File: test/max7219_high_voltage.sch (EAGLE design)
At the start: 11 parts, among them IC4 MAX7219CNG

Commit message: tschüüüüüs
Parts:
- removed NPN: 2N3904, transistor-npn:2N3904
- added NPN2: 2N3904, transistor-npn:2N3904
- added PNP1: 2N3906, transistor-pnp:2N3906
- added R2: 10k, resistor:R-EU_0204/7
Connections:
- new net N$6: NPN2.B, PNP1.C, R2.1
- net 3.3V: now also NPN2.E, R2.2; no longer NPN.E
- net N$1: now also NPN2.C; no longer NPN.C
- net N$2: now also PNP1.B; no longer NPN.B
- net VCC: now also PNP1.E

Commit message: Test Schematic updated
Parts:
- added G1: AB9V, battery:AB9V
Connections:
- new net N$5: G1.+, PNP.E, R1.1
- net VCC: now also G1.-; no longer PNP.E, R1.1
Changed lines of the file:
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@@
 <?xml version="1.0" encoding="utf-8"?>
 <!DOCTYPE eagle SYSTEM "eagle.dtd">
-<eagle version="9.6.2">
+<eagle version="9.0.1">
 <drawing>
 <settings>
@@
 <part name="C3" library="resistor" library_urn="urn:adsk.eagle:library:348" deviceset="C-EU" device="025-025X050" package3d_urn="urn:adsk.eagle:package:26151/1" value="10nF"/>
 <part name="GND10" library="SparkFun-PowerSymbols" library_urn="urn:adsk.eagle:library:530" deviceset="GND2" device=""/>
-<part name="18V" library="supply2" library_urn="urn:adsk.eagle:library:372" deviceset="VCC" device="" value="18V"/>
 <part name="PNP" library="transistor-pnp" deviceset="2N3906" device=""/>
 <part name="R1" library="resistor" library_urn="urn:adsk.eagle:library:348" deviceset="R-EU_" device="0204/7" package3d_urn="urn:adsk.eagle:package:25945/1" value="10k"/>
-<part name="18V1" library="supply2" library_urn="urn:adsk.eagle:library:372" deviceset="VCC" device="" value="18V"/>
 <part name="NPN1" library="transistor-npn" deviceset="2N3904" device=""/>
 <part name="GND3" library="SparkFun-PowerSymbols" library_urn="urn:adsk.eagle:library:530" deviceset="GND2" device=""/>
@@
 <part name="GND4" library="SparkFun-PowerSymbols" library_urn="urn:adsk.eagle:library:530" deviceset="GND2" device=""/>
 <part name="18V2" library="supply2" library_urn="urn:adsk.eagle:library:372" deviceset="VCC" device="" value="5V"/>
+<part name="G1" library="battery" library_urn="urn:adsk.eagle:library:109" deviceset="AB9V" device="" package3d_urn="urn:adsk.eagle:package:4600/1"/>
 </parts>
 <sheets>
@@
 <attribute name="VALUE" x="-217.9574" y="52.197" size="1.778" layer="96" rot="R270"/>
 </instance>
-<instance part="5V" gate="VCC" x="-205.74" y="60.96" smashed="yes">
-<attribute name="VALUE" x="-208.28" y="58.42" size="1.778" layer="96" rot="R90"/>
+<instance part="5V" gate="VCC" x="-198.12" y="53.34" smashed="yes" rot="R270">
+<attribute name="VALUE" x="-200.66" y="55.88" size="1.778" layer="96"/>
 </instance>
 <instance part="GND2" gate="G$1" x="-198.12" y="-33.02" smashed="yes">
@@
 <attribute name="VALUE" x="-225.298" y="53.34" size="1.778" layer="96" rot="R270" align="top-center"/>
 </instance>
-<instance part="18V" gate="G$1" x="-83.82" y="43.18" smashed="yes">
-<attribute name="VALUE" x="-85.725" y="46.355" size="1.778" layer="96"/>
-</instance>
 <instance part="PNP" gate="G$1" x="-86.36" y="33.02" smashed="yes">
-<attribute name="NAME" x="-96.52" y="40.64" size="1.778" layer="95"/>
-<attribute name="VALUE" x="-96.52" y="38.1" size="1.778" layer="96"/>
+<attribute name="NAME" x="-88.9" y="27.94" size="1.778" layer="95"/>
+<attribute name="VALUE" x="-88.9" y="35.56" size="1.778" layer="96"/>
 </instance>
 <instance part="R1" gate="G$1" x="-91.44" y="25.4" smashed="yes" rot="R90">
@@
 <attribute name="VALUE" x="-88.138" y="21.59" size="1.778" layer="96" rot="R90"/>
 </instance>
-<instance part="18V1" gate="G$1" x="-91.44" y="15.24" smashed="yes" rot="R180">
-<attribute name="VALUE" x="-89.535" y="12.065" size="1.778" layer="96" rot="R180"/>
-</instance>
 <instance part="NPN1" gate="G1" x="-99.06" y="33.02" smashed="yes">
-<attribute name="NAME" x="-109.22" y="40.64" size="1.778" layer="95"/>
-<attribute name="VALUE" x="-109.22" y="38.1" size="1.778" layer="96"/>
+<attribute name="NAME" x="-104.14" y="27.94" size="1.778" layer="95"/>
+<attribute name="VALUE" x="-104.14" y="35.56" size="1.778" layer="96"/>
 </instance>
 <instance part="GND3" gate="G$1" x="-99.06" y="22.86" smashed="yes" rot="R270">
@@
 <attribute name="VALUE" x="-98.425" y="5.715" size="1.778" layer="96"/>
 </instance>
+<instance part="G1" gate="G$1" x="-180.34" y="66.04"/>
 </instances>
 <busses>
@@
 <pinref part="5V" gate="VCC" pin="VCC"/>
 <pinref part="MODUL1" gate="MODUL" pin="+5V"/>
-<wire x1="-205.74" y1="58.42" x2="-205.74" y2="53.34" width="0.1524" layer="91"/>
+<wire x1="-200.66" y1="53.34" x2="-205.74" y2="53.34" width="0.1524" layer="91"/>
 <pinref part="C2" gate="G$1" pin="+"/>
 <wire x1="-205.74" y1="53.34" x2="-205.74" y2="43.18" width="0.1524" layer="91"/>
 <wire x1="-210.82" y1="53.34" x2="-205.74" y2="53.34" width="0.1524" layer="91"/>
 <junction x="-205.74" y="53.34"/>
-</segment>
-<segment>
-<wire x1="-91.44" y1="20.32" x2="-91.44" y2="17.78" width="0.1524" layer="91"/>
-<pinref part="R1" gate="G$1" pin="1"/>
-<junction x="-91.44" y="20.32"/>
-<pinref part="18V1" gate="G$1" pin="VCC"/>
-<junction x="-91.44" y="17.78"/>
-</segment>
-<segment>
-<pinref part="18V" gate="G$1" pin="VCC"/>
-<pinref part="PNP" gate="G$1" pin="E"/>
-<wire x1="-83.82" y1="40.64" x2="-83.82" y2="38.1" width="0.1524" layer="91"/>
-<junction x="-83.82" y="38.1"/>
-<junction x="-83.82" y="40.64"/>
+<wire x1="-205.74" y1="53.34" x2="-205.74" y2="66.04" width="0.1524" layer="91"/>
+<pinref part="G1" gate="G$1" pin="-"/>
+<wire x1="-205.74" y1="66.04" x2="-193.04" y2="66.04" width="0.1524" layer="91"/>
 </segment>
 <segment>
@@
 </segment>
 </net>
+<net name="N$5" class="0">
+<segment>
+<pinref part="G1" gate="G$1" pin="+"/>
+<wire x1="-167.64" y1="66.04" x2="-76.2" y2="66.04" width="0.1524" layer="91"/>
+<wire x1="-76.2" y1="66.04" x2="-76.2" y2="38.1" width="0.1524" layer="91"/>
+<pinref part="PNP" gate="G$1" pin="E"/>
+<wire x1="-76.2" y1="38.1" x2="-83.82" y2="38.1" width="0.1524" layer="91"/>
+<wire x1="-76.2" y1="38.1" x2="-76.2" y2="17.78" width="0.1524" layer="91"/>
+<junction x="-76.2" y="38.1"/>
+<wire x1="-91.44" y1="20.32" x2="-91.44" y2="17.78" width="0.1524" layer="91"/>
+<pinref part="R1" gate="G$1" pin="1"/>
+<junction x="-91.44" y="20.32"/>
+<wire x1="-76.2" y1="17.78" x2="-91.44" y2="17.78" width="0.1524" layer="91"/>
+</segment>
+</net>

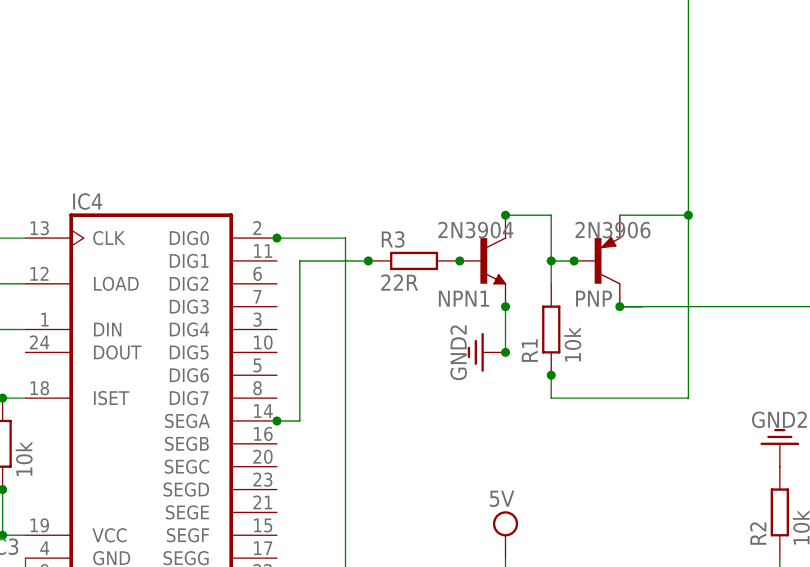
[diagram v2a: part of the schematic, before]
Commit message: test 2k2Ohm ansatt 220
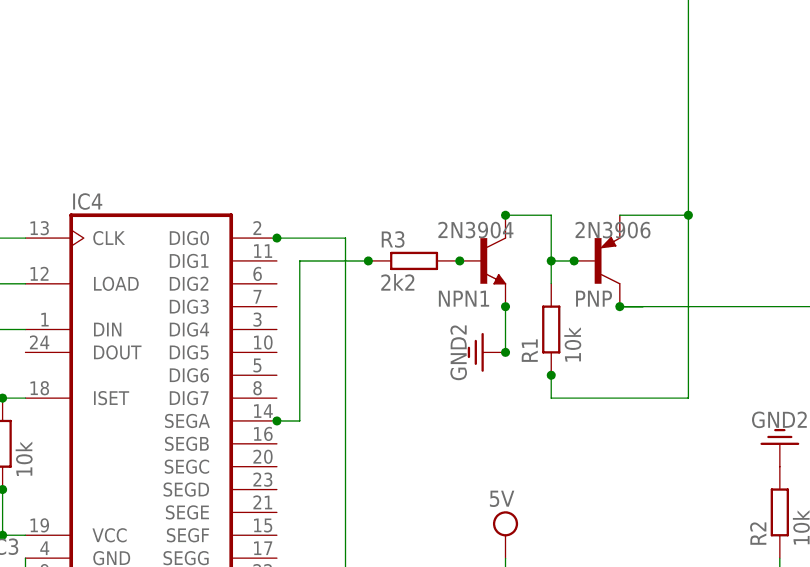
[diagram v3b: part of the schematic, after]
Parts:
- R3: value 22R -> 2k2
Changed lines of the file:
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@@
 <part name="NPN1" library="transistor-npn" deviceset="2N3904" device=""/>
 <part name="GND3" library="SparkFun-PowerSymbols" library_urn="urn:adsk.eagle:library:530" deviceset="GND2" device=""/>
-<part name="R3" library="resistor" library_urn="urn:adsk.eagle:library:348" deviceset="R-EU_" device="0204/7" package3d_urn="urn:adsk.eagle:package:25945/1" value="22R"/>
+<part name="R3" library="resistor" library_urn="urn:adsk.eagle:library:348" deviceset="R-EU_" device="0204/7" package3d_urn="urn:adsk.eagle:package:25945/1" value="2k2"/>
 <part name="PNP1" library="transistor-pnp" deviceset="2N3906" device=""/>
 <part name="NPN2" library="transistor-npn" deviceset="2N3904" device=""/>
